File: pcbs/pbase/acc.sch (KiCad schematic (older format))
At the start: 2 parts

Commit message: Test points
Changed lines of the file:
@@
 Text HLabel 5550 4100 0    60   Output ~ 0
 INT
-Text HLabel 5550 3700 0    60   BiDi ~ 0
+Text HLabel 7800 4150 2    60   BiDi ~ 0
 SDA0
-Text HLabel 5550 3600 0    60   BiDi ~ 0
+Text HLabel 7800 3600 2    60   BiDi ~ 0
 SCL0
 $Comp
@@
 Wire Wire Line
 	5000 4000 5750 4000
+Wire Wire Line
+	7400 3600 7800 3600
+Wire Wire Line
+	7400 4150 7800 4150
+Text Label 7400 3600 2    60   ~ 0
+SCL
+Text Label 7400 4150 2    60   ~ 0
+SDA
+Text Label 5550 3600 2    60   ~ 0
+SCL
+Text Label 5550 3700 2    60   ~ 0
+SDA
 $EndSCHEMATC

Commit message: cambios a sch
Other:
- note added: "LEER MPU9250 QUE TIENE MAGNETOMETRO"
- moved on the sheet: R?, U?
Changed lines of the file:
@@
 L ACC-MPU6050-GY521-BOARD U?
 U 1 1 5B95EA4E
-P 5950 3300
-F 0 "U?" H 6850 3700 60  0000 C CNN
-F 1 "ACC-MPU6050-GY521-BOARD" H 6050 3700 60  0000 C CNN
-F 2 "" H 5950 3250 60  0001 C CNN
-F 3 "" H 5950 3250 60  0001 C CNN
-	1    5950 3300
+P 5950 3250
+F 0 "U?" H 6850 3650 60  0000 C CNN
+F 1 "ACC-MPU6050-GY521-BOARD" H 6050 3650 60  0000 C CNN
+F 2 "" H 5950 3200 60  0001 C CNN
+F 3 "" H 5950 3200 60  0001 C CNN
+	1    5950 3250
 	1    0    0    -1
 $EndComp
 $Comp
-L +5V #PWR?
+L +5V #PWR08
 U 1 1 5B95EA92
-P 5550 3200
-F 0 "#PWR?" H 5550 3050 50  0001 C CNN
-F 1 "+5V" H 5550 3340 50  0000 C CNN
-F 2 "" H 5550 3200 50  0001 C CNN
-F 3 "" H 5550 3200 50  0001 C CNN
-	1    5550 3200
+P 5550 3150
+F 0 "#PWR08" H 5550 3000 50  0001 C CNN
+F 1 "+5V" H 5550 3290 50  0000 C CNN
+F 2 "" H 5550 3150 50  0001 C CNN
+F 3 "" H 5550 3150 50  0001 C CNN
+	1    5550 3150
 	1    0    0    -1
 $EndComp
 $Comp
-L GND #PWR?
+L GND #PWR09
 U 1 1 5B95EAA8
-P 5000 3650
-F 0 "#PWR?" H 5000 3400 50  0001 C CNN
-F 1 "GND" H 5000 3500 50  0000 C CNN
-F 2 "" H 5000 3650 50  0001 C CNN
-F 3 "" H 5000 3650 50  0001 C CNN
-	1    5000 3650
+P 5000 3600
+F 0 "#PWR09" H 5000 3350 50  0001 C CNN
+F 1 "GND" H 5000 3450 50  0000 C CNN
+F 2 "" H 5000 3600 50  0001 C CNN
+F 3 "" H 5000 3600 50  0001 C CNN
+	1    5000 3600
 	1    0    0    -1
 $EndComp
-NoConn ~ 5750 3800
-NoConn ~ 5750 3900
+NoConn ~ 5750 3750
+NoConn ~ 5750 3850
 $Comp
 L R R?
 U 1 1 5B95EC02
-P 5000 4300
-F 0 "R?" H 5150 4350 50  0000 C CNN
-F 1 "4.7K" H 5150 4250 50  0000 C CNN
-F 2 "" V 4930 4300 50  0001 C CNN
-F 3 "" H 5000 4300 50  0001 C CNN
-	1    5000 4300
+P 5000 4250
+F 0 "R?" H 5150 4300 50  0000 C CNN
+F 1 "4.7K" H 5150 4200 50  0000 C CNN
+F 2 "" V 4930 4250 50  0001 C CNN
+F 3 "" H 5000 4250 50  0001 C CNN
+	1    5000 4250
 	1    0    0    -1
 $EndComp
-Text HLabel 5550 4100 0    60   Output ~ 0
+Text HLabel 5550 4050 0    60   Output ~ 0
 INT
-Text HLabel 7800 4150 2    60   BiDi ~ 0
+Text HLabel 7200 3600 2    60   BiDi ~ 0
 SDA0
-Text HLabel 7800 3600 2    60   BiDi ~ 0
+Text HLabel 7200 3500 2    60   BiDi ~ 0
 SCL0
 $Comp
-L GND #PWR?
+L GND #PWR010
 U 1 1 5B95ED76
-P 5000 4450
-F 0 "#PWR?" H 5000 4200 50  0001 C CNN
-F 1 "GND" H 5000 4300 50  0000 C CNN
-F 2 "" H 5000 4450 50  0001 C CNN
-F 3 "" H 5000 4450 50  0001 C CNN
-	1    5000 4450
+P 5000 4400
+F 0 "#PWR010" H 5000 4150 50  0001 C CNN
+F 1 "GND" H 5000 4250 50  0000 C CNN
+F 2 "" H 5000 4400 50  0001 C CNN
+F 3 "" H 5000 4400 50  0001 C CNN
+	1    5000 4400
 	1    0    0    -1
 $EndComp
@@
 Acelerómetro
 Wire Wire Line
-	5750 3600 5550 3600
+	5750 3550 5550 3550
 Wire Wire Line
-	5750 3700 5550 3700
+	5750 3650 5550 3650
 Wire Wire Line
-	5750 4100 5550 4100
+	5750 4050 5550 4050
 Wire Wire Line
-	5750 3400 5550 3400
+	5750 3350 5550 3350
 Wire Wire Line
-	5550 3400 5550 3200
+	5550 3350 5550 3150
 Wire Wire Line
-	5750 3500 5000 3500
+	5750 3450 5000 3450
 Wire Wire Line
-	5000 3500 5000 3650
+	5000 3450 5000 3600
 Wire Wire Line
-	5000 4150 5000 4000
+	5000 4100 5000 3950
 Wire Wire Line
-	5000 4000 5750 4000
+	5000 3950 5750 3950
 Wire Wire Line
-	7400 3600 7800 3600
+	6800 3500 7200 3500
 Wire Wire Line
-	7400 4150 7800 4150
-Text Label 7400 3600 2    60   ~ 0
+	6800 3600 7200 3600
+Text Label 6800 3500 2    60   ~ 0
 SCL
-Text Label 7400 4150 2    60   ~ 0
+Text Label 6800 3600 2    60   ~ 0
 SDA
-Text Label 5550 3600 2    60   ~ 0
+Text Label 5550 3550 2    60   ~ 0
 SCL
-Text Label 5550 3700 2    60   ~ 0
+Text Label 5550 3650 2    60   ~ 0
 SDA
+Text Notes 7550 2900 0    60   ~ 0
+LEER MPU9250 QUE TIENE MAGNETOMETRO
 $EndSCHEMATC

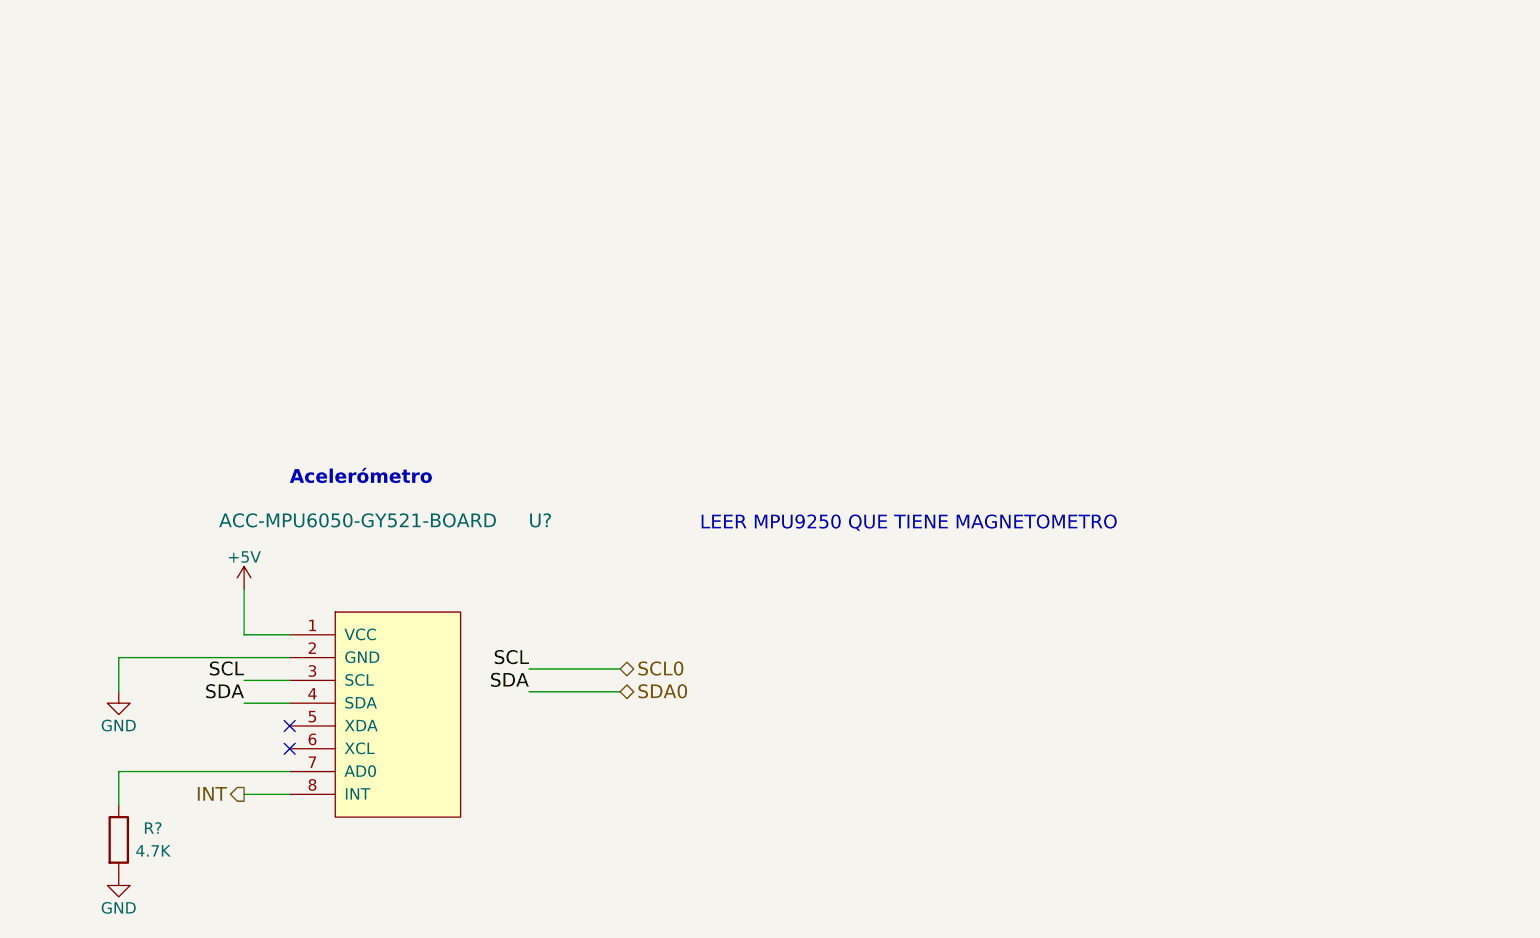
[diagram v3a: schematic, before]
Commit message: modificaciones varias al acc mpu-6050
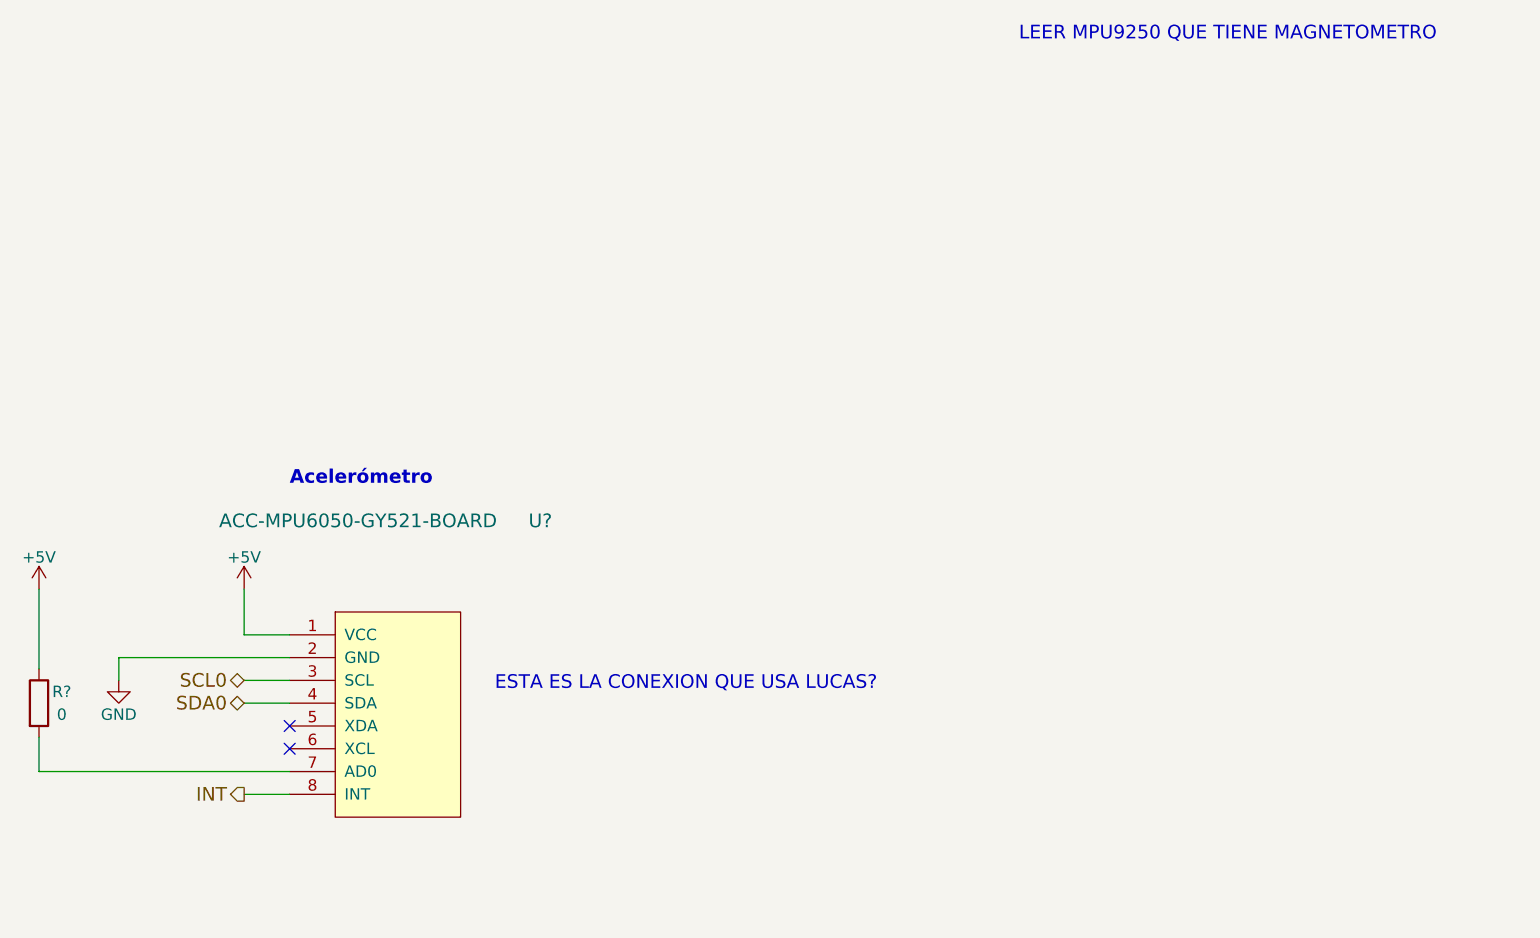
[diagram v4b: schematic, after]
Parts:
- removed R?: 4.7K, symbol R
- removed U?: ACC-MPU6050-GY521-BOARD, symbol ACC-MPU6050-GY521-BOARD
- added R?: 0, symbol R
- added U?: ACC-MPU6050-GY521-BOARD, symbol ACC-MPU6050-GY521-BOARD
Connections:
- net +5V: now also R?.1, U?.1 (VCC)
- net GND: now also U?.2 (GND)
- net INT: now also U?.8 (INT)
- net SCL0: now also U?.3 (SCL)
- net SDA0: now also U?.4 (SDA)
- new net: R?.2, U?.7 (AD0)
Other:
- note added: "ESTA ES LA CONEXION QUE USA LUCAS?"
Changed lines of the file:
@@
 $EndDescr
-$Comp
-L ACC-MPU6050-GY521-BOARD U?
-U 1 1 5B95EA4E
-P 5950 3250
-F 0 "U?" H 6850 3650 60  0000 C CNN
-F 1 "ACC-MPU6050-GY521-BOARD" H 6050 3650 60  0000 C CNN
-F 2 "" H 5950 3200 60  0001 C CNN
-F 3 "" H 5950 3200 60  0001 C CNN
-	1    5950 3250
-	1    0    0    -1
-$EndComp
 $Comp
 L +5V #PWR08
@@
 L GND #PWR09
 U 1 1 5B95EAA8
-P 5000 3600
-F 0 "#PWR09" H 5000 3350 50  0001 C CNN
-F 1 "GND" H 5000 3450 50  0000 C CNN
-F 2 "" H 5000 3600 50  0001 C CNN
-F 3 "" H 5000 3600 50  0001 C CNN
-	1    5000 3600
+P 5000 3550
+F 0 "#PWR09" H 5000 3300 50  0001 C CNN
+F 1 "GND" H 5000 3400 50  0000 C CNN
+F 2 "" H 5000 3550 50  0001 C CNN
+F 3 "" H 5000 3550 50  0001 C CNN
+	1    5000 3550
 	1    0    0    -1
 $EndComp
 NoConn ~ 5750 3750
 NoConn ~ 5750 3850
-$Comp
-L R R?
-U 1 1 5B95EC02
-P 5000 4250
-F 0 "R?" H 5150 4300 50  0000 C CNN
-F 1 "4.7K" H 5150 4200 50  0000 C CNN
-F 2 "" V 4930 4250 50  0001 C CNN
-F 3 "" H 5000 4250 50  0001 C CNN
-	1    5000 4250
-	1    0    0    -1
-$EndComp
 Text HLabel 5550 4050 0    60   Output ~ 0
 INT
-Text HLabel 7200 3600 2    60   BiDi ~ 0
+Text HLabel 5550 3650 0    60   BiDi ~ 0
 SDA0
-Text HLabel 7200 3500 2    60   BiDi ~ 0
+Text HLabel 5550 3550 0    60   BiDi ~ 0
 SCL0
-$Comp
-L GND #PWR010
-U 1 1 5B95ED76
-P 5000 4400
-F 0 "#PWR010" H 5000 4150 50  0001 C CNN
-F 1 "GND" H 5000 4250 50  0000 C CNN
-F 2 "" H 5000 4400 50  0001 C CNN
-F 3 "" H 5000 4400 50  0001 C CNN
-	1    5000 4400
-	1    0    0    -1
-$EndComp
 Text Notes 5750 2700 0    60   ~ 12
 Acelerómetro
@@
 	5750 3450 5000 3450
 Wire Wire Line
-	5000 3450 5000 3600
+	5000 3450 5000 3550
+Text Notes 8950 750  0    60   ~ 0
+LEER MPU9250 QUE TIENE MAGNETOMETRO
+Text Notes 6650 3600 0    60   ~ 0
+ESTA ES LA CONEXION QUE USA LUCAS?
+$Comp
+L R R?
+U 1 1 5B9EFBEB
+P 4650 3650
+F 0 "R?" H 4750 3700 50  0000 C CNN
+F 1 "0" H 4750 3600 50  0000 C CNN
+F 2 "" V 4580 3650 50  0001 C CNN
+F 3 "" H 4650 3650 50  0001 C CNN
+	1    4650 3650
+	1    0    0    -1
+$EndComp
 Wire Wire Line
-	5000 4100 5000 3950
+	5750 3950 4650 3950
 Wire Wire Line
-	5000 3950 5750 3950
+	4650 3950 4650 3800
 Wire Wire Line
-	6800 3500 7200 3500
-Wire Wire Line
-	6800 3600 7200 3600
-Text Label 6800 3500 2    60   ~ 0
-SCL
-Text Label 6800 3600 2    60   ~ 0
-SDA
-Text Label 5550 3550 2    60   ~ 0
-SCL
-Text Label 5550 3650 2    60   ~ 0
-SDA
-Text Notes 7550 2900 0    60   ~ 0
-LEER MPU9250 QUE TIENE MAGNETOMETRO
+	4650 3500 4650 3150
+$Comp
+L +5V #PWR?
+U 1 1 5B9EFC38
+P 4650 3150
+F 0 "#PWR?" H 4650 3000 50  0001 C CNN
+F 1 "+5V" H 4650 3290 50  0000 C CNN
+F 2 "" H 4650 3150 50  0001 C CNN
+F 3 "" H 4650 3150 50  0001 C CNN
+	1    4650 3150
+	1    0    0    -1
+$EndComp
+$Comp
+L ACC-MPU6050-GY521-BOARD U?
+U 1 1 5B9F1FCA
+P 5950 3250
+F 0 "U?" H 6850 3650 60  0000 C CNN
+F 1 "ACC-MPU6050-GY521-BOARD" H 6050 3650 60  0000 C CNN
+F 2 "" H 5950 3200 60  0001 C CNN
+F 3 "" H 5950 3200 60  0001 C CNN
+	1    5950 3250
+	1    0    0    -1
+$EndComp
 $EndSCHEMATC

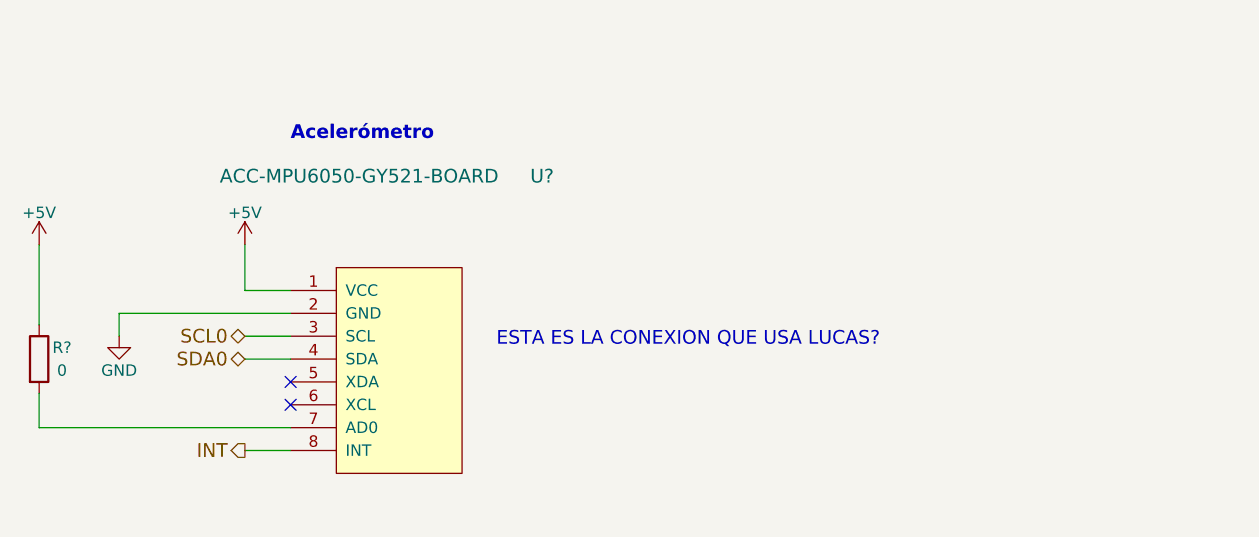
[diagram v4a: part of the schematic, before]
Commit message: reemplazado acc por mpu9250
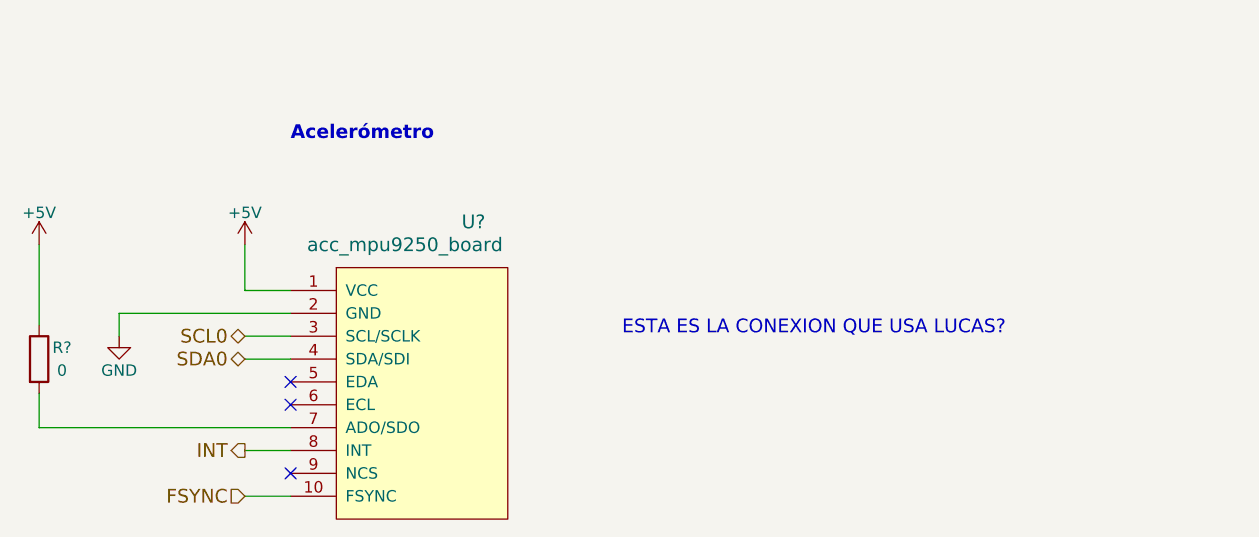
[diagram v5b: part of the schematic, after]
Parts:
- removed U?: ACC-MPU6050-GY521-BOARD, symbol ACC-MPU6050-GY521-BOARD
- added U?: acc_mpu9250_board, symbol acc_mpu9250_board
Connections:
- net +5V: now also U?.1 (VCC)
- net GND: now also U?.2 (GND)
- net INT: now also U?.8 (INT)
- net SCL0: now also U?.3 (SCL/SCLK)
- net SDA0: now also U?.4 (SDA/SDI)
- net at R?.2: now also U?.7 (ADO/SDO)
- new net FSYNC: U?.10 (FSYNC)
- no-connect marks 2 -> 3
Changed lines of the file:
@@
 LIBS:lpcxpresso_lpc1769_revb
 LIBS:gps_em506
+LIBS:acc_mpu9250_board
 LIBS:pbase-cache
 EELAYER 25 0
@@
 Text Notes 8950 750  0    60   ~ 0
 LEER MPU9250 QUE TIENE MAGNETOMETRO
-Text Notes 6650 3600 0    60   ~ 0
+Text Notes 7200 3550 0    60   ~ 0
 ESTA ES LA CONEXION QUE USA LUCAS?
 $Comp
@@
 $EndComp
 $Comp
-L ACC-MPU6050-GY521-BOARD U?
-U 1 1 5B9F1FCA
+L acc_mpu9250_board U?
+U 1 1 5B9F28BB
 P 5950 3250
-F 0 "U?" H 6850 3650 60  0000 C CNN
-F 1 "ACC-MPU6050-GY521-BOARD" H 6050 3650 60  0000 C CNN
-F 2 "" H 5950 3200 60  0001 C CNN
-F 3 "" H 5950 3200 60  0001 C CNN
+F 0 "U?" H 6550 3450 60  0000 C CNN
+F 1 "acc_mpu9250_board" H 6250 3350 60  0000 C CNN
+F 2 "" H 5950 3250 60  0001 C CNN
+F 3 "" H 5950 3250 60  0001 C CNN
 	1    5950 3250
 	1    0    0    -1
 $EndComp
+NoConn ~ 5750 4150
+Text HLabel 5550 4250 0    60   Input ~ 0
+FSYNC
+Wire Wire Line
+	5550 4250 5750 4250
 $EndSCHEMATC

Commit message: sch annotate v1.1
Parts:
- R1: renamed from R?; value 0 -> 0R
- gave numbers to parts that had none: 1
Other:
- note removed: "ESTA ES LA CONEXION QUE USA LUCAS?"
- note removed: "LEER MPU9250 QUE TIENE MAGNETOMETRO"
- moved on the sheet: R1, U2
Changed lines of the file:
@@
 Rev "A"
 Comp "UTN - FRBA"
-Comment1 ""
-Comment2 ""
-Comment3 ""
-Comment4 ""
+Comment1 "Si FSYNC no se usa ponerlo a GND o en LOW."
+Comment2 "R1 es un jumper. Quitarlo si se desea conservar la dirección que trae por defecto."
+Comment3 "Misma conexión que el MPU6050."
+Comment4 "Este acelerómetro ya incorpora un magnetómetro."
 $EndDescr
 $Comp
-L +5V #PWR08
+L +5V #PWR10
 U 1 1 5B95EA92
-P 5550 3150
-F 0 "#PWR08" H 5550 3000 50  0001 C CNN
-F 1 "+5V" H 5550 3290 50  0000 C CNN
-F 2 "" H 5550 3150 50  0001 C CNN
-F 3 "" H 5550 3150 50  0001 C CNN
-	1    5550 3150
+P 5600 3250
+F 0 "#PWR10" H 5600 3100 50  0001 C CNN
+F 1 "+5V" H 5600 3390 50  0000 C CNN
+F 2 "" H 5600 3250 50  0001 C CNN
+F 3 "" H 5600 3250 50  0001 C CNN
+	1    5600 3250
 	1    0    0    -1
 $EndComp
 $Comp
-L GND #PWR09
+L GND #PWR9
 U 1 1 5B95EAA8
-P 5000 3550
-F 0 "#PWR09" H 5000 3300 50  0001 C CNN
-F 1 "GND" H 5000 3400 50  0000 C CNN
-F 2 "" H 5000 3550 50  0001 C CNN
-F 3 "" H 5000 3550 50  0001 C CNN
-	1    5000 3550
+P 5050 3650
+F 0 "#PWR9" H 5050 3400 50  0001 C CNN
+F 1 "GND" H 5050 3500 50  0000 C CNN
+F 2 "" H 5050 3650 50  0001 C CNN
+F 3 "" H 5050 3650 50  0001 C CNN
+	1    5050 3650
 	1    0    0    -1
 $EndComp
-NoConn ~ 5750 3750
-NoConn ~ 5750 3850
-Text HLabel 5550 4050 0    60   Output ~ 0
+NoConn ~ 5800 3850
+NoConn ~ 5800 3950
+Text HLabel 5600 4150 0    60   Output ~ 0
 INT
-Text HLabel 5550 3650 0    60   BiDi ~ 0
+Text HLabel 5600 3750 0    60   BiDi ~ 0
 SDA0
-Text HLabel 5550 3550 0    60   BiDi ~ 0
+Text HLabel 5600 3650 0    60   BiDi ~ 0
 SCL0
-Text Notes 5750 2700 0    60   ~ 12
+Text Notes 5800 2800 0    60   ~ 12
 Acelerómetro
 Wire Wire Line
-	5750 3550 5550 3550
+	5800 3650 5600 3650
 Wire Wire Line
-	5750 3650 5550 3650
+	5800 3750 5600 3750
 Wire Wire Line
-	5750 4050 5550 4050
+	5800 4150 5600 4150
 Wire Wire Line
-	5750 3350 5550 3350
+	5800 3450 5600 3450
 Wire Wire Line
-	5550 3350 5550 3150
+	5600 3450 5600 3250
 Wire Wire Line
-	5750 3450 5000 3450
+	5800 3550 5050 3550
 Wire Wire Line
-	5000 3450 5000 3550
-Text Notes 8950 750  0    60   ~ 0
-LEER MPU9250 QUE TIENE MAGNETOMETRO
-Text Notes 7200 3550 0    60   ~ 0
-ESTA ES LA CONEXION QUE USA LUCAS?
+	5050 3550 5050 3650
 $Comp
-L R R?
+L R R1
 U 1 1 5B9EFBEB
-P 4650 3650
-F 0 "R?" H 4750 3700 50  0000 C CNN
-F 1 "0" H 4750 3600 50  0000 C CNN
-F 2 "" V 4580 3650 50  0001 C CNN
-F 3 "" H 4650 3650 50  0001 C CNN
-	1    4650 3650
+P 4700 3750
+F 0 "R1" H 4800 3800 50  0000 C CNN
+F 1 "0R" H 4800 3700 50  0000 C CNN
+F 2 "" V 4630 3750 50  0001 C CNN
+F 3 "" H 4700 3750 50  0001 C CNN
+	1    4700 3750
 	1    0    0    -1
 $EndComp
 Wire Wire Line
-	5750 3950 4650 3950
+	5800 4050 4700 4050
 Wire Wire Line
-	4650 3950 4650 3800
+	4700 4050 4700 3900
 Wire Wire Line
-	4650 3500 4650 3150
+	4700 3600 4700 3250
 $Comp
-L +5V #PWR?
+L +5V #PWR8
 U 1 1 5B9EFC38
-P 4650 3150
-F 0 "#PWR?" H 4650 3000 50  0001 C CNN
-F 1 "+5V" H 4650 3290 50  0000 C CNN
-F 2 "" H 4650 3150 50  0001 C CNN
-F 3 "" H 4650 3150 50  0001 C CNN
-	1    4650 3150
+P 4700 3250
+F 0 "#PWR8" H 4700 3100 50  0001 C CNN
+F 1 "+5V" H 4700 3390 50  0000 C CNN
+F 2 "" H 4700 3250 50  0001 C CNN
+F 3 "" H 4700 3250 50  0001 C CNN
+	1    4700 3250
 	1    0    0    -1
 $EndComp
 $Comp
-L acc_mpu9250_board U?
+L acc_mpu9250_board U2
 U 1 1 5B9F28BB
-P 5950 3250
-F 0 "U?" H 6550 3450 60  0000 C CNN
-F 1 "acc_mpu9250_board" H 6250 3350 60  0000 C CNN
-F 2 "" H 5950 3250 60  0001 C CNN
-F 3 "" H 5950 3250 60  0001 C CNN
-	1    5950 3250
+P 6000 3350
+F 0 "U2" H 6600 3550 60  0000 C CNN
+F 1 "acc_mpu9250_board" H 6300 3450 60  0000 C CNN
+F 2 "" H 6000 3350 60  0001 C CNN
+F 3 "" H 6000 3350 60  0001 C CNN
+	1    6000 3350
 	1    0    0    -1
 $EndComp
-NoConn ~ 5750 4150
-Text HLabel 5550 4250 0    60   Input ~ 0
+NoConn ~ 5800 4250
+Text HLabel 5600 4350 0    60   Input ~ 0
 FSYNC
 Wire Wire Line
-	5550 4250 5750 4250
+	5600 4350 5800 4350
 $EndSCHEMATC
